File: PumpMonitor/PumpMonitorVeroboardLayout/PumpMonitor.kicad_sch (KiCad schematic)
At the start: 29 parts, among them J1 Power & Current Sense, J2 Programming, J3 Ra01_Breakout_Module, Q1 BC548, Q2 BC548, SW1 SW_Push, U1 LM317_TO-220, U2 24LC16, U3 PICAXE-18M2

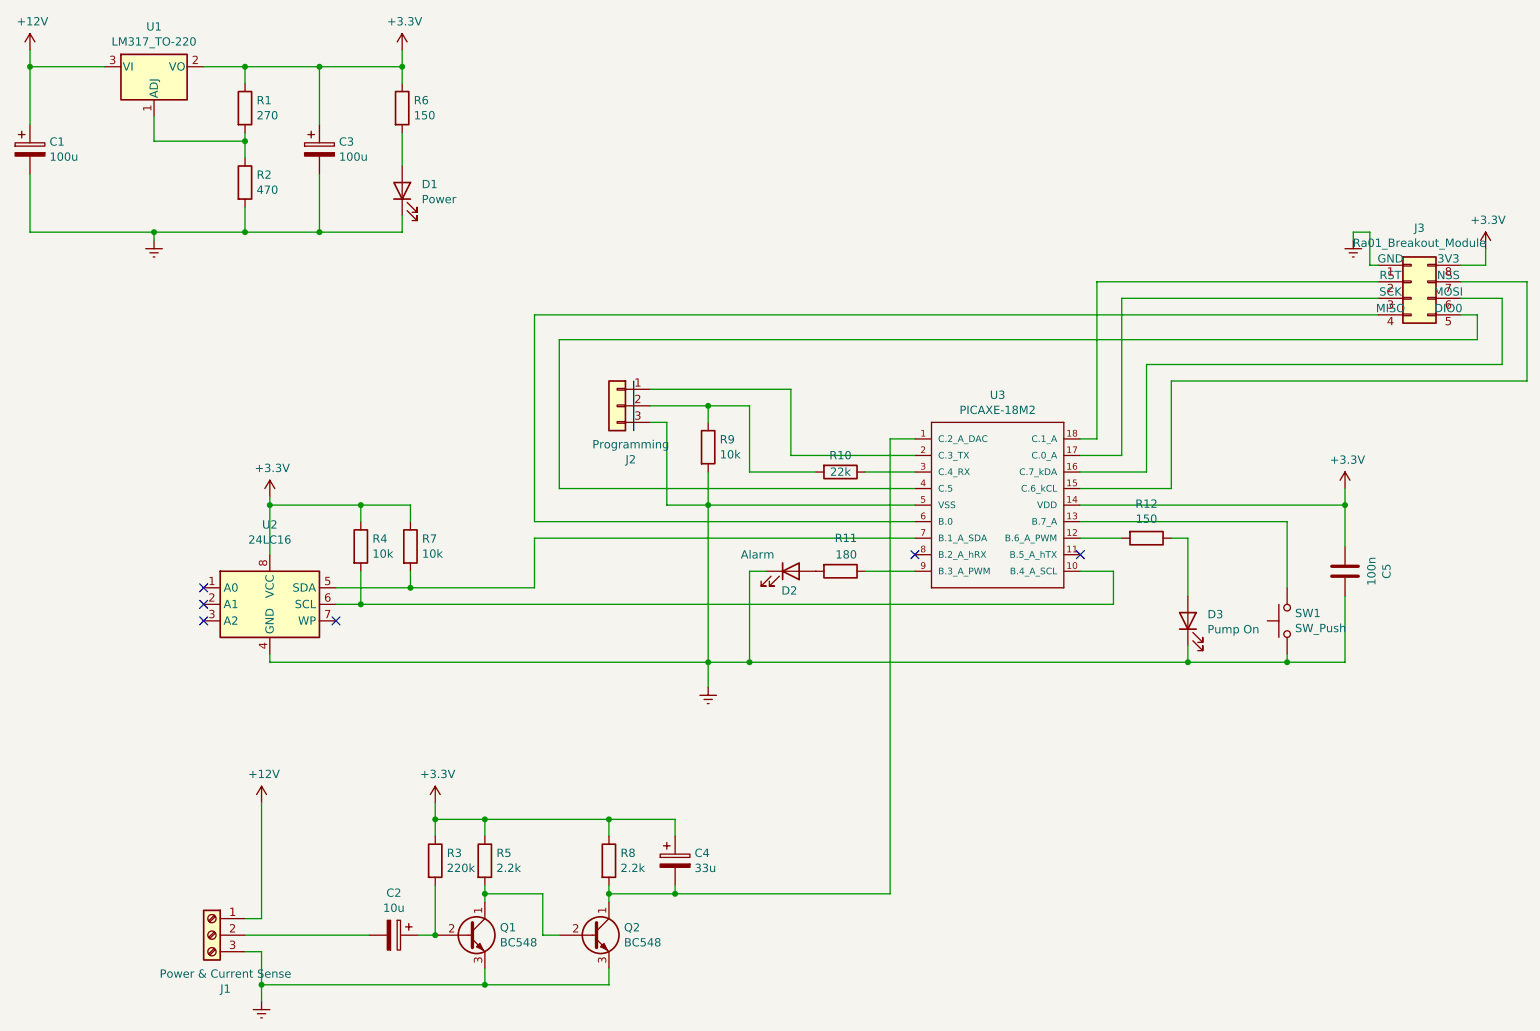
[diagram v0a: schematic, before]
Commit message: Added temperature sensor CRC check
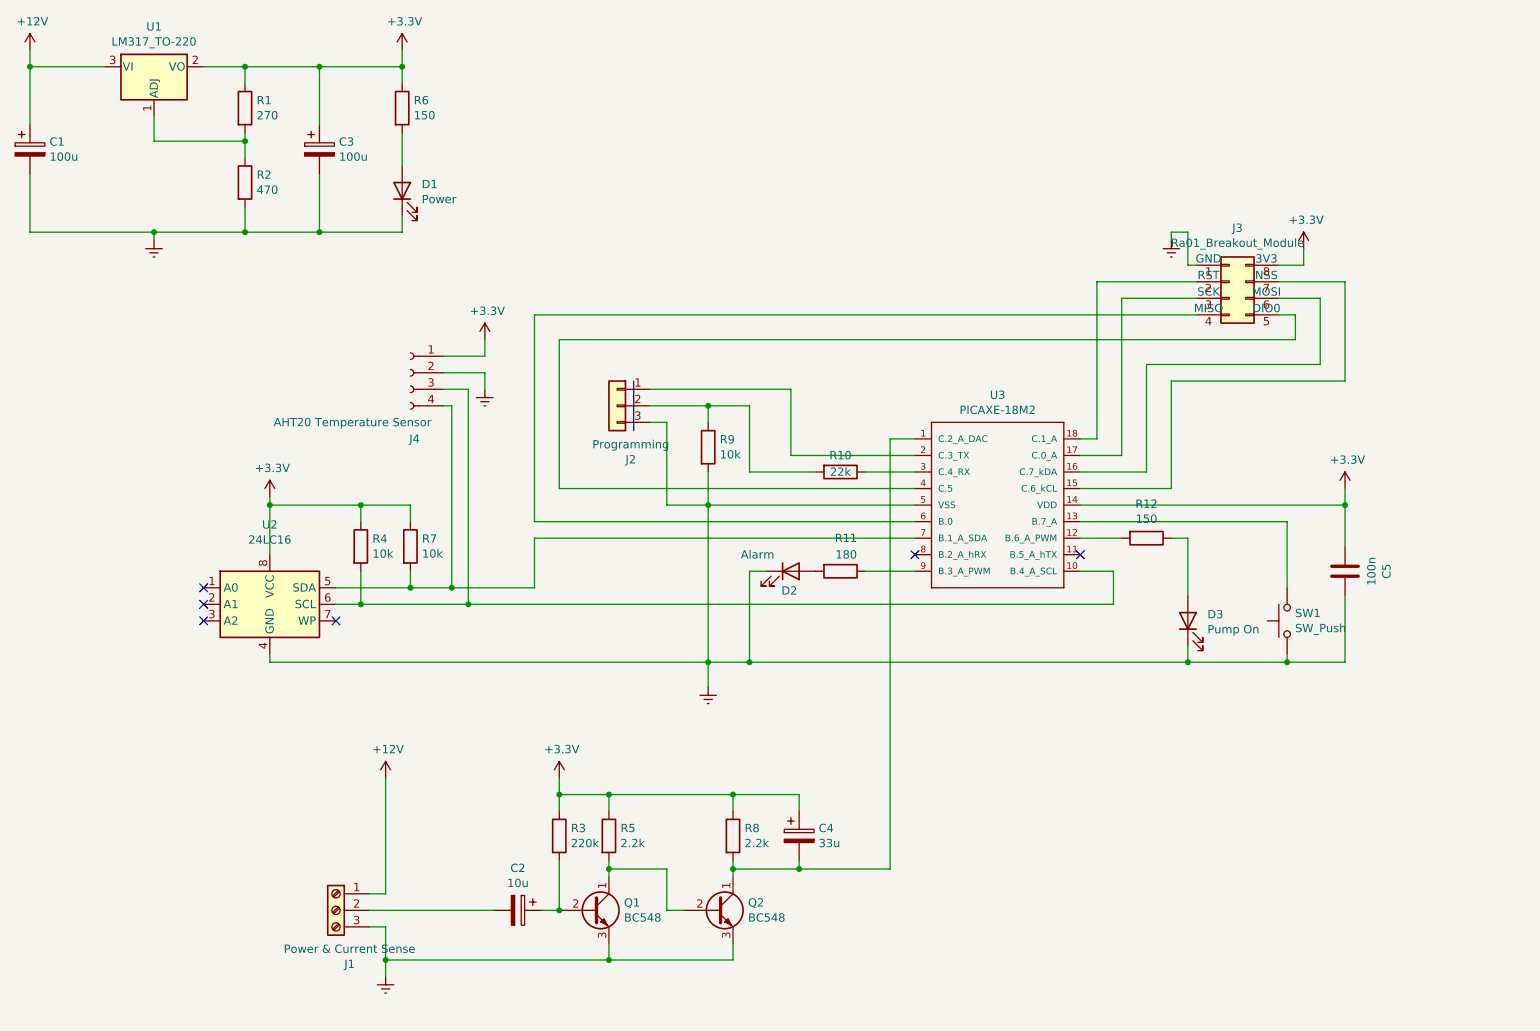
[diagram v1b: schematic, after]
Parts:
- added J4: AHT20 Temperature Sensor, Connector_PinHeader_2.54mm:PinHeader_1x04_P2.54mm_Vertical, symbol Connector:Conn_01x04_Socket
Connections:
- net +3V3: now also J4.1 (Pin_1)
- net Earth: now also J4.2 (Pin_2)
- net at R4.2, U2.6 (SCL), U3.10 (B.4_A_SCL): now also J4.3 (Pin_3)
- net at R7.2, U2.5 (SDA), U3.7 (B.1_A_SDA): now also J4.4 (Pin_4)
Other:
- moved on the sheet: C2, C4, J1, J3, Q1, Q2, R3, R5, R8

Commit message: Updated battery and pump monitor KiCAD files to be openable
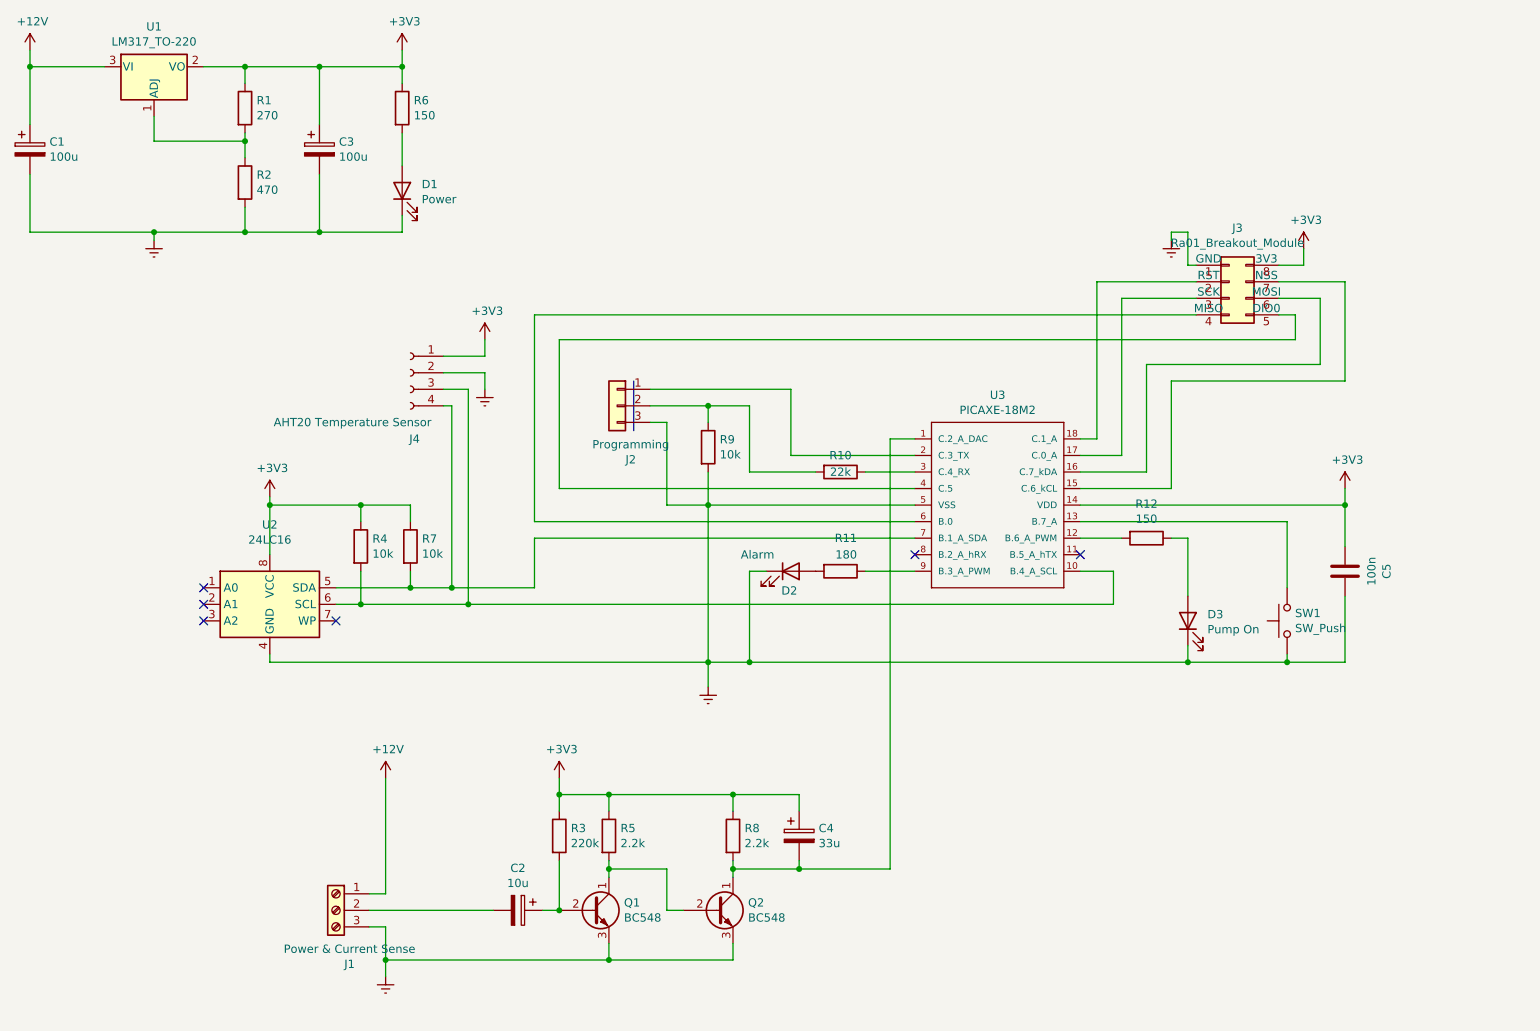
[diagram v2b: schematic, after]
